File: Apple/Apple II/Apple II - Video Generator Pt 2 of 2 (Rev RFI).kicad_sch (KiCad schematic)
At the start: 0 parts

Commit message: Finished Apple II - Sheet 20 - Video Generator Part 2 (Rev RFI)
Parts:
- added A14, A? (x2): 74LS02, symbol Apple II:A14_74LS02
- added A?: 74LS02, symbol Apple II:A12_74LS02
- added B? (x4): 74LS02, symbol Apple II:B14_74LS02
- added B?: 74LS02, symbol Apple II:B13_74LS02
- added B?: 74LS08, symbol Apple II:B11_74LS08
- added B?: 74LS11, symbol Apple II:B12_74LS11
- added C13, C14: 0.1µF, symbol Device:C_Small
- added C16, C2: 47pF, symbol Device:C_Small
- added C3: 5-50pF, symbol Device:C_Variable
- added C?: 74LS32, symbol Apple II:C14_74LS32
- added C?: 74LS04, symbol Apple II:C11_74LS04
- added J250: AUX VIDEO PIN, symbol Connector:Conn_01x02_Male
- added J?: AUX VIDEO CONNECTOR, symbol Connector:Conn_01x04_Male
- added J?: COMPOSITE VIDEO OUTPUT, symbol Connector:Conn_Coaxial
- added JP?: 12, symbol Apple II:Bowtie_SolderJumper
- added JP?: 14, symbol Jumper:SolderJumper_2_Open
- added JP?: 16, symbol Apple II:Bowtie_SolderJumper
- added JP?: 13, symbol Jumper:SolderJumper_2_Open
- added L1, L7: 27µH, symbol Device:L
- added Q3, Q6: 2N3904, Package_TO_SOT_THT:TO-92_Inline, symbol Transistor_BJT:2N3904
- added R10: 27Ω, symbol Device:R_US
- added R11: 200Ω, symbol Device:R_Potentiometer_US
- added R27: 4.7K, symbol Device:R_US
- added R5: 1K, symbol Device:R_US
- added R6: 2.7K, symbol Device:R_US
- added R7: 1.5K, symbol Device:R_US
- added R8: 2K, symbol Device:R_US
- added R9: 10Ω, symbol Device:R_US
- added U? (x2): C13_74LS51, symbol Apple II:C13_74LS51
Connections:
- new net: B?.11, JP?.2 (B), JP?.2 (B)
- new net: A?.4, B?.12
- new net: B?.13, U?.12
- new net: B?.1, B?.1
- new net: A?.1, B?.2
- new net: A?.13, B?.3, U?.10
- new net: A14.10, B?.3
- new net: A14.4, A14.8
- new net: Q3.3 (C), R9.1
- new net: J250.1 (Pin_1), R10.1, R11.2
- new net: L7.1, R10.2
- new net: B?.8, C?.4, U?.13
- new net: B?.1, U?.1
- new net: B?.2, JP?.2 (B), JP?.2 (B)
- new net: C?.10, JP?.1 (A)
- new net: A14.5, A14.6, B?.4
- new net: A?.5, A?.6, B?.10
- new net: J?.2 (Pin_2), Q3.1 (E), R11.1
- new net: Q3.2 (B), R6.2, R7.2, R8.2
- new net: C2.1, C3.1, L1.1, Q6.3 (C), R5.2, R6.1
- new net: C16.1, J?.1 (In), L7.2
- new net: Q6.2 (B), R27.2
- new net +12V: C14.1, J?.4 (Pin_4)
- new net +5V: R9.2
- new net -5V: C13.1, J?.3 (Pin_3)
- new net AN2: J250.2 (Pin_2)
- new net BLANKING: C?.6
- new net COLOR_BURST: B?.12, R5.1
- new net COLOR_REF_{35}: A?.3
- new net Earth: C13.2, C14.2, C16.2, C2.2, C3.2, J?.1 (Pin_1), J?.2 (Ext), L1.2, Q6.1 (E), R11.3
- new net H2: A?.11, A?.12
- new net H3: A14.9, B?.2, U?.11, U?.3
- new net H4: B?.5, U?.2
- new net H5: B?.6, U?.4, U?.5
- new net HBL: B?.13, C?.5, U?.6, U?.9
- new net SYNC_{19}: R8.1, U?.8
- new net TEXT MODE: A?.2, R27.1
- new net V0: B?.9
- new net V1: JP?.1 (A)
- new net V2: C?.11, JP?.1 (A)
- new net V3: B?.9
- new net V4: B?.10
- new net V5: JP?.1 (A)
- new net VC: B?.8
- new net VIDEO_DATA: R7.1
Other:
- note added: "FROM CLOCK GENERATOR"
- note added: "FROM ON-BOARD I/O"
- note added: "FROM ON-BOARD I/O PT1"
- note added: "FROM PART 1"
- note added: "FROM VIDEO ADDRESS GENERATOR"
- note added: "TO MEMORY ADDRESS PT 1"
- note added: "TO PART 1"
- note added: "TO PERIPHREAL I/O"
- title: (none) -> Apple II - Video Generator Part 2

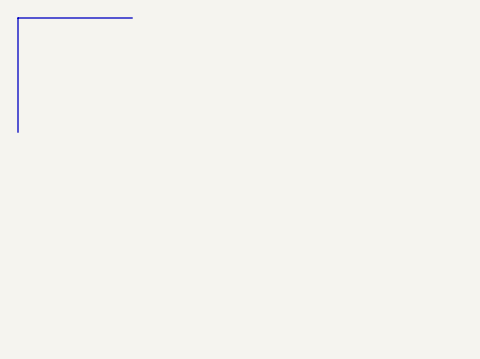
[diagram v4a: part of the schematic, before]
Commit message: Finished Apple II - Sheet 22 - Two-Piece Keyboard
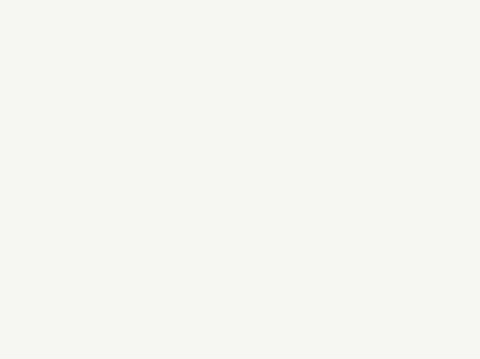
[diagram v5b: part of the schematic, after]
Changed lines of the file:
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@@
     (stroke (width 0) (type solid) (color 0 0 0 0))
-  )
-  (polyline (pts (xy 12.7 0) (xy 0 0))
-    (stroke (width 0) (type default) (color 0 0 0 0))
   )
   (wire (pts (xy 363.22 134.62) (xy 363.22 137.16))
@@
     (stroke (width 0) (type default) (color 0 0 0 0))
   )
-  (polyline (pts (xy 0 0) (xy 0 12.7))
-    (stroke (width 0) (type default) (color 0 0 0 0))
-  )
